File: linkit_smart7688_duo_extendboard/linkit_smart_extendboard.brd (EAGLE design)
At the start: 100 x 78 mm, 29 parts, among them U1 BME280

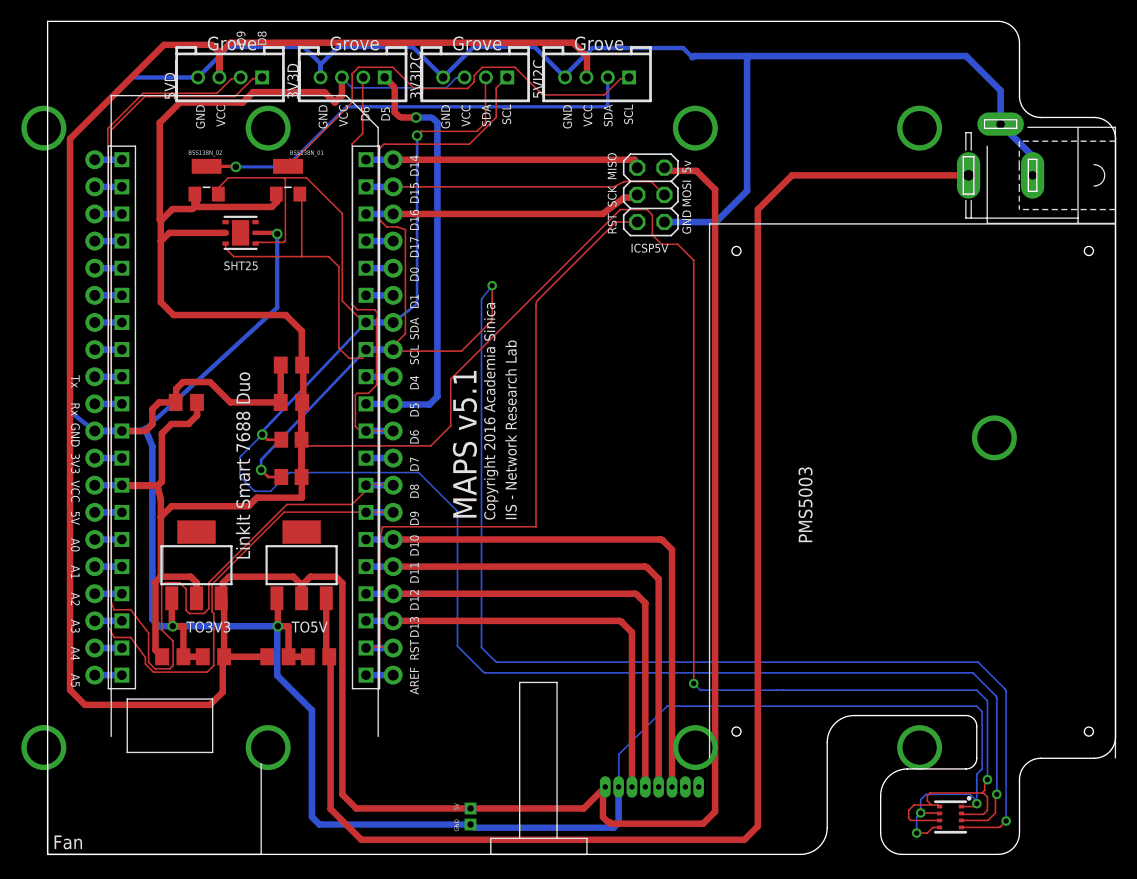
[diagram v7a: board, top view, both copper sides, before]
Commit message: update PCB layout & RP1135C piercing 3D design
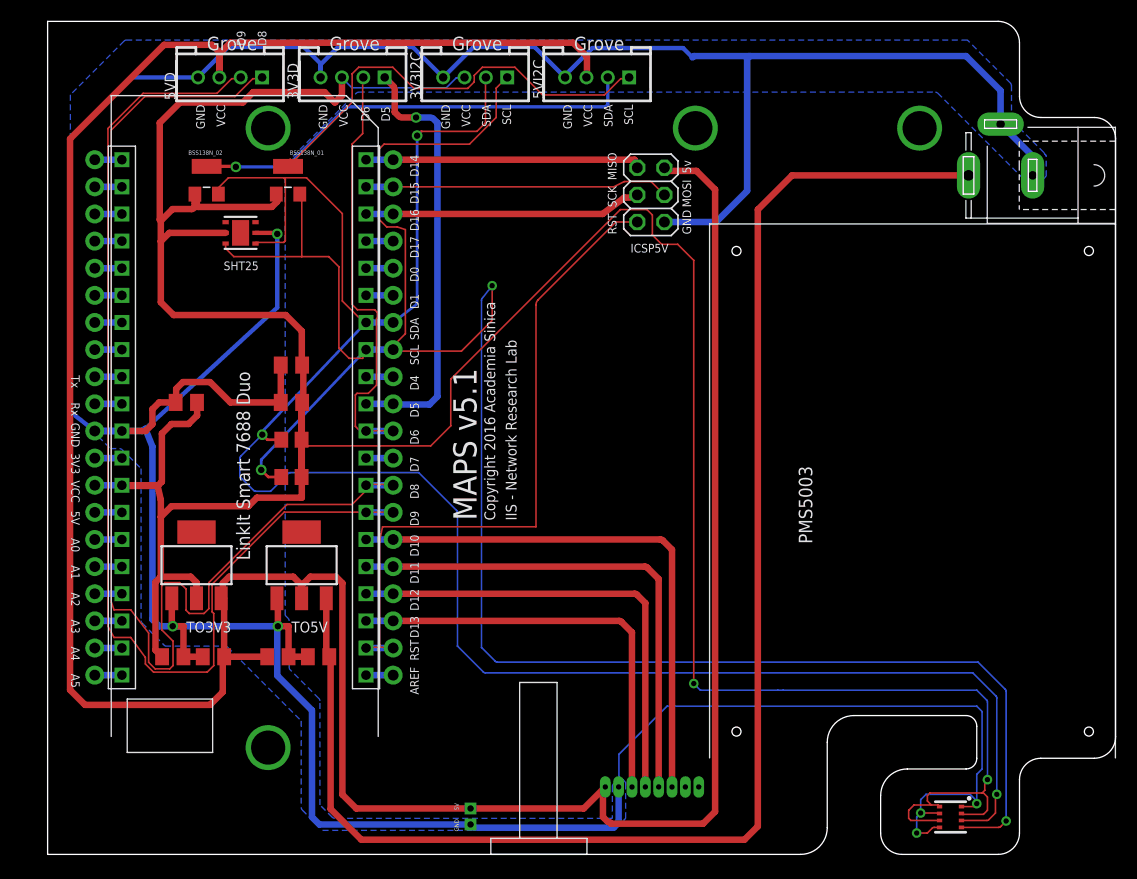
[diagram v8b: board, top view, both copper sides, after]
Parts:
- removed U$5: (no value), fan_2_2:FAN
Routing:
- added copper zone on layer 16, net GND
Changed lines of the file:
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@@
 <layer number="112" name="tSilk" color="7" fill="1" visible="yes" active="yes"/>
 <layer number="113" name="ReferenceLS" color="7" fill="1" visible="no" active="no"/>
-<layer number="114" name="howlong" color="40" fill="1" visible="yes" active="yes"/>
+<layer number="114" name="howlong" color="40" fill="1" visible="no" active="yes"/>
 <layer number="116" name="Patch_BOT" color="7" fill="1" visible="yes" active="yes"/>
 <layer number="118" name="Rect_Pads" color="7" fill="1" visible="yes" active="yes"/>
@@
 <element name="U$2" library="G5" package="G5" value="" x="99.9825" y="9.0325" smashed="yes" rot="R180"/>
 <element name="U$4" library="pin_2mm" package="PIN2MM" value="PIN2MM" x="39.1" y="4.8" smashed="yes" rot="R270"/>
-<element name="U$5" library="fan_2_2" package="FAN" value="" x="0" y="0"/>
 <element name="U$6" library="sma" package="SMA" value="" x="41.5" y="0"/>
 </elements>
@@
 <wire x1="82.82810625" y1="2.45310625" x2="82.375" y2="2" width="0.1524" layer="1"/>
 <wire x1="82.375" y1="2" x2="81.375" y2="2" width="0.1524" layer="1"/>
+<polygon width="0.4064" layer="16" isolate="0.254">
+<vertex x="93.375" y="65.5" curve="44.99958"/>
+<vertex x="93.2866125" y="65.7133875"/>
+<vertex x="90.25" y="68.75"/>
+<vertex x="90.25" y="71.9934875" curve="45"/>
+<vertex x="90.15700625" y="72.21799375"/>
+<vertex x="86.125" y="76.25"/>
+<vertex x="7.3815125" y="76.25" curve="45"/>
+<vertex x="7.15700625" y="76.15700625"/>
+<vertex x="2.125" y="71.125"/>
+<vertex x="2.125" y="41.8815125" curve="45"/>
+<vertex x="2.21799375" y="41.65700625"/>
+<vertex x="5.875" y="38"/>
+<vertex x="6.7434875" y="38" curve="-45"/>
+<vertex x="6.96799375" y="37.90700625"/>
+<vertex x="8.75" y="36.125"/>
+<vertex x="8.75" y="21.8815125" curve="45"/>
+<vertex x="8.84299375" y="21.65700625"/>
+<vertex x="11" y="19.5"/>
+<vertex x="16.6184875" y="19.5" curve="-45"/>
+<vertex x="16.84299375" y="19.40700625"/>
+<vertex x="23.75" y="12.5"/>
+<vertex x="23.75" y="4.3815125" curve="45"/>
+<vertex x="23.84299375" y="4.15700625"/>
+<vertex x="25.75" y="2.25"/>
+<vertex x="52.8684875" y="2.25" curve="45"/>
+<vertex x="53.09299375" y="2.34299375"/>
+<vertex x="54.125" y="3.375"/>
+<vertex x="54.125" y="6.6184875" curve="45"/>
+<vertex x="54.03200625" y="6.84299375"/>
+<vertex x="53.75" y="7.125"/>
+<vertex x="53.46799375" y="6.84299375" curve="-45"/>
+<vertex x="53.2434875" y="6.75"/>
+<vertex x="53.125" y="6.75"/>
+<vertex x="52.96799375" y="6.59299375" curve="45"/>
+<vertex x="52.875" y="6.3684875"/>
+<vertex x="52.875" y="3.375"/>
+<vertex x="26.8815125" y="3.375" curve="-45"/>
+<vertex x="26.65700625" y="3.46799375"/>
+<vertex x="25.5" y="4.625"/>
+<vertex x="25.5" y="14.3684875" curve="45"/>
+<vertex x="25.40700625" y="14.59299375"/>
+<vertex x="22.625" y="17.375"/>
+<vertex x="22.625" y="21.8684875" curve="45"/>
+<vertex x="22.53200625" y="22.09299375"/>
+<vertex x="22.25" y="22.375"/>
+<vertex x="22.25" y="64.4934875" curve="-45"/>
+<vertex x="22.34299375" y="64.71799375"/>
+<vertex x="25.625" y="68"/>
+<vertex x="28.90700625" y="71.28200625" curve="-45"/>
+<vertex x="29.1315125" y="71.375"/>
+<vertex x="79.625" y="71.375"/>
+<vertex x="83.1184875" y="71.375" curve="-45"/>
+<vertex x="83.34299375" y="71.28200625"/>
+<vertex x="91.375" y="63.25"/>
+<vertex x="93.1184875" y="63.25" curve="45"/>
+<vertex x="93.34299375" y="63.34299375"/>
+<vertex x="93.5" y="63.5"/>
+<vertex x="93.5" y="65.5"/>
+</polygon>
 </signal>
 <signal name="N$10">
@@
 <contactref element="PMS3003" pad="2"/>
 </signal>
-<signal name="1" airwireshidden="yes">
-<via x="88.65" y="39" extent="1-16" drill="3.2" diameter="2.54"/>
-</signal>
 <signal name="S$1">
 </signal>
@@
 </signal>
 <signal name="S$4">
-</signal>
-<signal name="S$5">
-<via x="81.65" y="10" extent="1-16" drill="3.2" diameter="2.54"/>
 </signal>
 <signal name="S$6">
@@
 <via x="60.65" y="68" extent="1-16" drill="3.2" diameter="0.254"/>
 </signal>
-<signal name="S$10">
-<via x="60.65" y="10" extent="1-16" drill="3.2" diameter="0.254"/>
-</signal>
-<signal name="S$11">
-<via x="-0.35" y="68" extent="1-16" drill="3.2" diameter="0.254"/>
-</signal>
-<signal name="S$12">
-<via x="-0.35" y="10" extent="1-16" drill="3.2" diameter="0.254"/>
-</signal>
 </signals>
